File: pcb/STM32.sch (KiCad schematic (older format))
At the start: 32 parts, among them J1 Conn_02x07_Odd_Even, Q5 2SC3325-Y, X1 ABM8G

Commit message: Added all connections between STM and AQH3223. added pin header with GPIO from STM
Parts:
- added J3: Conn_02x11_Odd_Even, Connector_PinHeader_2.54mm:PinHeader_2x11_P2.54mm_Vertical, symbol Connector_Generic:Conn_02x11_Odd_Even
- J1: value Conn_02x07_Odd_Even -> Conn_02x04_Odd_Even; footprint Connector_PinSocket_2.54mm:PinSocket_2x07_P2.54mm_Horizontal -> Connector_PinSocket_2.54mm:PinSocket_2x04_P2.54mm_Horizontal; symbol Connector_Generic:Conn_02x07_Odd_Even -> Connector_Generic:Conn_02x04_Odd_Even
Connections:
- net +3V3: now also J3.1 (Pin_1)
- net +5V: now also J3.2 (Pin_2)
- net GND: now also J1.7 (Pin_7), J1.8 (Pin_8), J3.20 (Pin_20), J3.21 (Pin_21), J3.22 (Pin_22); no longer J1.13 (Pin_13), J1.14 (Pin_14)
- net LED: now also UST1.7 (PC13); no longer UST1.48 (PB11/I2C2_SDA/USART3_TX/TIM2_CH4)
- net PA10: now also J3.17 (Pin_17); no longer J1.10 (Pin_10)
- net PA11: now also J3.18 (Pin_18); no longer J1.11 (Pin_11)
- net PA12: now also J3.19 (Pin_19); no longer J1.12 (Pin_12)
- net PA8: now also J3.15 (Pin_15); no longer J1.8 (Pin_8)
- net PA9: now also J3.16 (Pin_16); no longer J1.9 (Pin_9)
- net PC9: now also J3.14 (Pin_14); no longer J1.7 (Pin_7)
- net P_EV7: now reaches UST1.38 (PE7)
- net PD8: now reaches UST1.55 (PD8/USART3_TX)
- net PD8: now also J3.3 (Pin_3)
- net PD9: now reaches UST1.56 (PD9/USART3_RX)
- net PD9: now also J3.4 (Pin_4)
- net PD10: now reaches UST1.57 (PD10/USART3_CK)
- net PD10: now also J3.5 (Pin_5)
- net PD11: now reaches UST1.58 (PD11/USART3_CTS)
- net PD11: now also J3.6 (Pin_6)
- net PD12: now reaches UST1.59 (PD12/TIM4_CH1/USART3_RTS)
- net PD12: now also J3.7 (Pin_7)
- net PD13: now reaches UST1.60 (PD13/TIM4_CH2)
- net PD13: now also J3.8 (Pin_8)
- net PD14: now reaches UST1.61 (PD14/TIM4_CH3)
- net PD14: now also J3.9 (Pin_9)
- net PD15: now reaches UST1.62 (PD15/TIM4_CH4)
- net PD15: now also J3.10 (Pin_10)
- net PC6: now reaches UST1.63 (PC6/TIM8_CH1/SDIO_D6/USART6_TX//TIM3_CH1)
- net PC6: now also J3.11 (Pin_11)
- net PC7: now reaches UST1.64 (PC7/TIM8_CH2/SDIO_D7/USART6_RX/TIM3_CH2)
- net PC7: now also J3.12 (Pin_12)
- net PC8: now reaches UST1.65 (PC8/TIM8_CH3/SDIO_D0/TIM3_CH3/USART6_CK)
- net PC8: now also J3.13 (Pin_13)
- net PE0 renamed P_EV15
- net PE1 renamed P_EV14
- net PE2 renamed P_EV13
- net PE3 renamed P_EV12
- net PE4 renamed P_EV11
- net PE5 renamed P_EV10
- net PE6 renamed P_EV9
- net PE7 renamed P_EV8
- new net P_EV16: UST1.48 (PB11/I2C2_SDA/USART3_TX/TIM2_CH4)
- no-connect marks 30 -> 17
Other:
- moved on the sheet: FB1, R46, R47, R48, R49

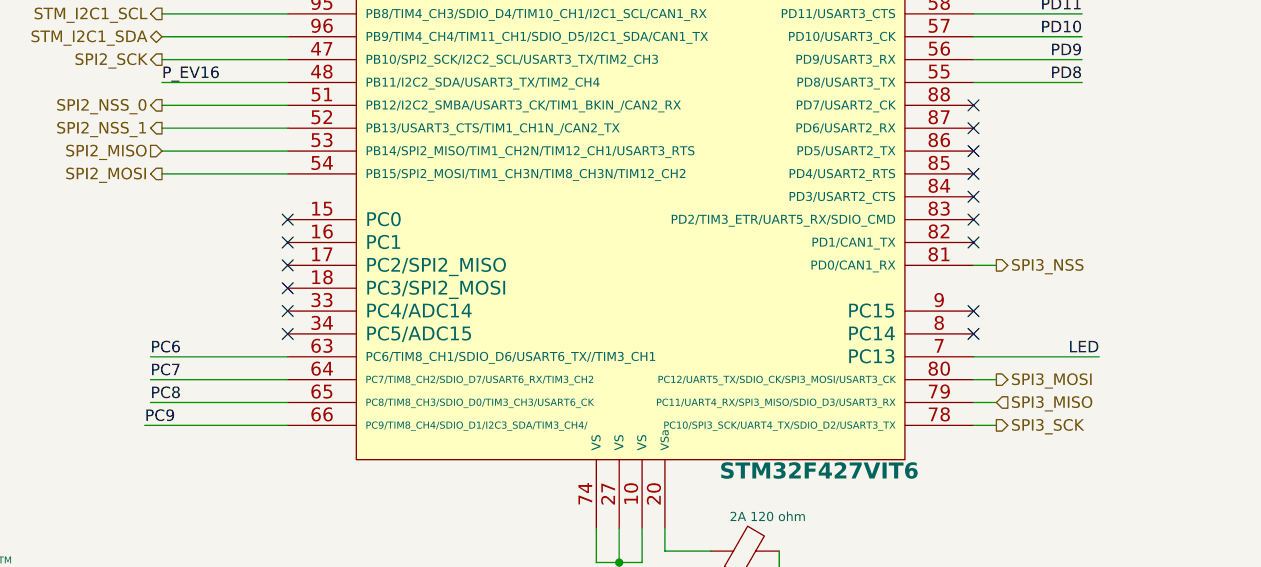
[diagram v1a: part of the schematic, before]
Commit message: Added 3d shape for connector clik-mate Added connection between STM and connector clik-mate on schema and PCB P3 is a connector that allows put a panic button for do a reset in the IC powerstep01
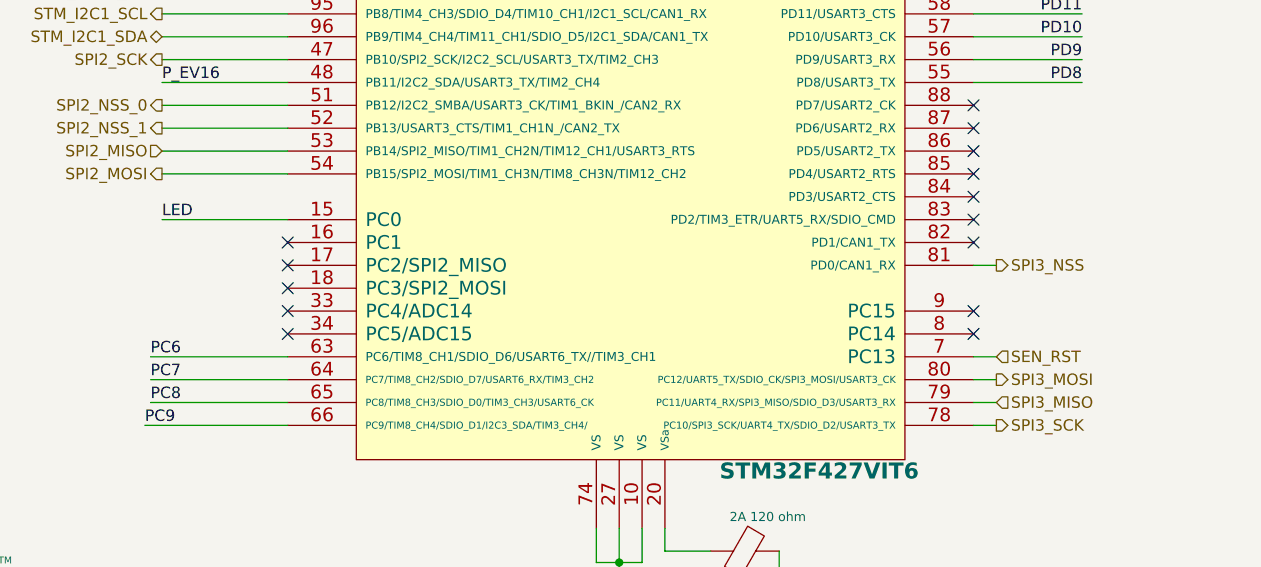
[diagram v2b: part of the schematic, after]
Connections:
- net LED: now also UST1.15 (PC0); no longer UST1.7 (PC13)
- new net SEN_RST: UST1.7 (PC13)
- no-connect marks 17 -> 16
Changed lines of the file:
@@
 NoConn ~ 5600 5600
 NoConn ~ 5600 5700
-NoConn ~ 2600 5200
 NoConn ~ 2600 5300
 NoConn ~ 2600 5400
@@
 $EndComp
 Wire Wire Line
-	5600 5800 6150 5800
-Text Label 6150 5800 2    50   ~ 0
+	2600 5200 2050 5200
+Text Label 2050 5200 0    50   ~ 0
 LED
 Entry Wire Line
@@
 	10325 3850 10325 3950
 Connection ~ 10325 3950
+Text HLabel 5700 5800 2    50   Input ~ 0
+SEN_RST
+Wire Wire Line
+	5700 5800 5600 5800
 Wire Bus Line
 	1800 6950 1800 7200

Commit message: Added components dikey part numbers in modified sheets
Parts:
- C29, C30, C38, CS1, CS2, CS3, CST1: DigiKey (none) -> 1276-1442-1-ND
- C39, CST2: DigiKey (none) -> 1276-1010-1-ND
- C40: DigiKey (none) -> 1276-1044-1-ND
- CST3, CST4: DigiKey (none) -> 1276-1469-1-ND
- CXST1, CXST2: DigiKey (none) -> 1276-1116-1-ND
- FB1, LST1, LST2: DigiKey (none) -> 445-2982-1-ND
- R25: DigiKey (none) -> P1.0KJCT-ND
- R46, R47, R48, R49: DigiKey (none) -> P100LCT-ND
- R54: DigiKey (none) -> P180JCT-ND
- RST1, RST2: DigiKey (none) -> 311-10KJRCT-ND
- X1: DigiKey (none) -> 535-14512-1-ND
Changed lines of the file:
@@
 F 2 "Capacitor_SMD:C_0402_1005Metric" H 1750 9050 60  0001 C CNN
 F 3 "" H 1750 9050 60  0001 C CNN
+F 4 "1276-1442-1-ND" H 1750 9050 50  0001 C CNN "DigiKey"
 	1    1750 9050
 	1    0    0    -1
@@
 F 2 "Capacitor_SMD:C_1206_3216Metric" H 3150 9050 60  0001 C CNN
 F 3 "" H 3150 9050 60  0001 C CNN
+F 4 "1276-1044-1-ND" H 3150 9050 50  0001 C CNN "DigiKey"
 	1    3150 9050
 	1    0    0    -1
@@
 F 2 "Capacitor_SMD:C_0603_1608Metric" H 2800 9050 60  0001 C CNN
 F 3 "" H 2800 9050 60  0001 C CNN
+F 4 "1276-1010-1-ND" H 2800 9050 50  0001 C CNN "DigiKey"
 	1    2800 9050
 	1    0    0    -1
@@
 F 2 "Capacitor_SMD:C_0402_1005Metric" H 2450 9050 60  0001 C CNN
 F 3 "" H 2450 9050 60  0001 C CNN
+F 4 "1276-1442-1-ND" H 2450 9050 50  0001 C CNN "DigiKey"
 	1    2450 9050
 	1    0    0    -1
@@
 F 2 "Capacitor_SMD:C_0402_1005Metric" H 2100 9050 60  0001 C CNN
 F 3 "" H 2100 9050 60  0001 C CNN
+F 4 "1276-1442-1-ND" H 2100 9050 50  0001 C CNN "DigiKey"
 	1    2100 9050
 	1    0    0    -1
@@
 F 2 "Capacitor_SMD:C_0402_1005Metric" H 1100 9050 60  0001 C CNN
 F 3 "" H 1100 9050 60  0001 C CNN
+F 4 "1276-1442-1-ND" H 1100 9050 50  0001 C CNN "DigiKey"
 	1    1100 9050
 	1    0    0    -1
@@
 F 2 "Capacitor_SMD:C_0402_1005Metric" H 1450 9050 60  0001 C CNN
 F 3 "" H 1450 9050 60  0001 C CNN
+F 4 "1276-1442-1-ND" H 1450 9050 50  0001 C CNN "DigiKey"
 	1    1450 9050
 	1    0    0    -1
@@
 F 2 "Capacitor_SMD:C_0402_1005Metric" H 7100 1950 60  0001 C CNN
 F 3 "" H 7100 1950 60  0001 C CNN
+F 4 "1276-1116-1-ND" H 7100 1950 50  0001 C CNN "DigiKey"
 	1    7100 1950
 	0    -1   -1   0
@@
 F 2 "Capacitor_SMD:C_0402_1005Metric" H 7100 1350 60  0001 C CNN
 F 3 "" H 7100 1350 60  0001 C CNN
+F 4 "1276-1116-1-ND" H 7100 1350 50  0001 C CNN "DigiKey"
 	1    7100 1350
 	0    -1   -1   0
@@
 F 2 "Resistor_SMD:R_0603_1608Metric" H 1050 850 60  0001 C CNN
 F 3 "" H 1050 850 60  0001 C CNN
+F 4 "445-2982-1-ND" V 1050 850 50  0001 C CNN "DigiKey"
 	1    1050 850
 	0    -1   -1   0
@@
 F 2 "Capacitor_SMD:C_0402_1005Metric" H 1350 950 60  0001 C CNN
 F 3 "" H 1350 950 60  0001 C CNN
+F 4 "1276-1442-1-ND" H 1350 950 50  0001 C CNN "DigiKey"
 	1    1350 950
 	1    0    0    -1
@@
 F 2 "Capacitor_SMD:C_0402_1005Metric" H 1750 950 60  0001 C CNN
 F 3 "" H 1750 950 60  0001 C CNN
+F 4 "1276-1010-1-ND" H 1750 950 50  0001 C CNN "DigiKey"
 	1    1750 950
 	1    0    0    -1
@@
 F 2 "Capacitor_SMD:C_0402_1005Metric" H 6200 1100 60  0001 C CNN
 F 3 "" H 6200 1100 60  0001 C CNN
+F 4 "1276-1469-1-ND" H 6200 1100 50  0001 C CNN "DigiKey"
 	1    6200 1100
 	1    0    0    -1
@@
 F 2 "Resistor_SMD:R_0402_1005Metric" H 1300 7450 60  0001 C CNN
 F 3 "" H 1300 7450 60  0001 C CNN
+F 4 "311-10KJRCT-ND" V 1300 7450 50  0001 C CNN "DigiKey"
 	1    1300 7450
 	-1   0    0    1
@@
 F 2 "Resistor_SMD:R_0402_1005Metric" H 1300 7050 60  0001 C CNN
 F 3 "" H 1300 7050 60  0001 C CNN
+F 4 "311-10KJRCT-ND" V 1300 7050 50  0001 C CNN "DigiKey"
 	1    1300 7050
 	-1   0    0    -1
@@
 F 2 "Capacitor_SMD:C_0402_1005Metric" H 6000 1100 60  0001 C CNN
 F 3 "" H 6000 1100 60  0001 C CNN
+F 4 "1276-1469-1-ND" H 6000 1100 50  0001 C CNN "DigiKey"
 	1    6000 1100
 	1    0    0    -1
@@
 F 2 "Capacitor_SMD:C_0402_1005Metric" H 3500 9050 60  0001 C CNN
 F 3 "" H 3500 9050 60  0001 C CNN
+F 4 "1276-1442-1-ND" H 3500 9050 50  0001 C CNN "DigiKey"
 	1    3500 9050
 	1    0    0    -1
@@
 F 2 "Resistor_SMD:R_0603_1608Metric" V 10405 2075 50  0001 C CNN
 F 3 "~" H 10475 2075 50  0001 C CNN
+F 4 "445-2982-1-ND" V 10475 2075 50  0001 C CNN "DigiKey"
 	1    10475 2075
 	0    1    1    0
@@
 F 2 "Resistor_SMD:R_0603_1608Metric" H 4600 6650 60  0001 C CNN
 F 3 "" H 4600 6650 60  0001 C CNN
+F 4 "445-2982-1-ND" V 4600 6650 50  0001 C CNN "DigiKey"
 	1    4600 6650
 	0    -1   -1   0
@@
 F 2 "SMD:ABM8G" H 6750 1650 50  0001 C CNN
 F 3 "" H 6750 1650 50  0001 C CNN
+F 4 "535-14512-1-ND" V 6750 1650 50  0001 C CNN "DigiKey"
 	1    6750 1650
 	0    -1   -1   0
@@
 F 2 "Resistor_SMD:R_0402_1005Metric" V 9430 4750 50  0001 C CNN
 F 3 "~" H 9500 4750 50  0001 C CNN
+F 4 "P100LCT-ND" V 9500 4750 50  0001 C CNN "DigiKey"
 	1    9500 4750
 	0    1    1    0
@@
 F 2 "Resistor_SMD:R_0402_1005Metric" V 9430 4650 50  0001 C CNN
 F 3 "~" H 9500 4650 50  0001 C CNN
+F 4 "P100LCT-ND" V 9500 4650 50  0001 C CNN "DigiKey"
 	1    9500 4650
 	0    1    1    0
@@
 F 2 "Resistor_SMD:R_0402_1005Metric" V 10580 4750 50  0001 C CNN
 F 3 "~" H 10650 4750 50  0001 C CNN
+F 4 "P100LCT-ND" V 10650 4750 50  0001 C CNN "DigiKey"
 	1    10650 4750
 	0    1    1    0
@@
 F 2 "Resistor_SMD:R_0402_1005Metric" V 10580 4650 50  0001 C CNN
 F 3 "~" H 10650 4650 50  0001 C CNN
+F 4 "P100LCT-ND" V 10650 4650 50  0001 C CNN "DigiKey"
 	1    10650 4650
 	0    1    1    0
@@
 F 2 "Resistor_SMD:R_0402_1005Metric" V 9055 6475 50  0001 C CNN
 F 3 "~" H 9125 6475 50  0001 C CNN
+F 4 "P180JCT-ND" V 9125 6475 50  0001 C CNN "DigiKey"
 	1    9125 6475
 	0    1    1    0
@@
 F 2 "Resistor_SMD:R_0402_1005Metric" V 10630 5725 50  0001 C CNN
 F 3 "~" H 10700 5725 50  0001 C CNN
-F 4 "" V 10700 5725 50  0001 C CNN "DigiKey"
+F 4 "P1.0KJCT-ND" V 10700 5725 50  0001 C CNN "DigiKey"
 	1    10700 5725
 	0    1    1    0
@@
 F 2 "Connector_PinHeader_2.54mm:PinHeader_2x11_P2.54mm_Vertical" H 10025 3450 50  0001 C CNN
 F 3 "~" H 10025 3450 50  0001 C CNN
+F 4 "" H 10025 3450 50  0001 C CNN "DigiKey"
 	1    10025 3450
 	1    0    0    -1

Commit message: Added digiKey part number for some components
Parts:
- J3: DigiKey (none) -> S2012EC-40-ND
- RST1, RST2: DigiKey 311-10KJRCT-ND -> P10KJDKR-ND
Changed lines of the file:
@@
 F 2 "Resistor_SMD:R_0402_1005Metric" H 1300 7450 60  0001 C CNN
 F 3 "" H 1300 7450 60  0001 C CNN
-F 4 "311-10KJRCT-ND" V 1300 7450 50  0001 C CNN "DigiKey"
+F 4 "P10KJDKR-ND" V 1300 7450 50  0001 C CNN "DigiKey"
 	1    1300 7450
 	-1   0    0    1
@@
 F 2 "Resistor_SMD:R_0402_1005Metric" H 1300 7050 60  0001 C CNN
 F 3 "" H 1300 7050 60  0001 C CNN
-F 4 "311-10KJRCT-ND" V 1300 7050 50  0001 C CNN "DigiKey"
+F 4 "P10KJDKR-ND" V 1300 7050 50  0001 C CNN "DigiKey"
 	1    1300 7050
 	-1   0    0    -1
@@
 F 2 "Connector_PinHeader_2.54mm:PinHeader_2x11_P2.54mm_Vertical" H 10025 3450 50  0001 C CNN
 F 3 "~" H 10025 3450 50  0001 C CNN
-F 4 "" H 10025 3450 50  0001 C CNN "DigiKey"
+F 4 "S2012EC-40-ND" H 10025 3450 50  0001 C CNN "DigiKey"
 	1    10025 3450
 	1    0    0    -1

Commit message: Added all references on silkscreen added BOM for sensor modules
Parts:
- J1: DigiKey (none) -> 609-6367-ND‎
- LS1: DigiKey (none) -> 102-2196-1-ND; Field4 None -> (none); Field5 CUI -> (none); Field6 None -> (none); Field7 Unavailable -> (none)
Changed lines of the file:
@@
 F 2 "Connector_PinSocket_2.54mm:PinSocket_2x04_P2.54mm_Horizontal" H 10025 4650 50  0001 C CNN
 F 3 "~" H 10025 4650 50  0001 C CNN
+F 4 "609-6367-ND‎" H 10025 4650 50  0001 C CNN "DigiKey"
 	1    10025 4650
 	1    0    0    -1
@@
 F 2 "SMD:CUI_CSS-95B30-SMT" H 9525 5900 50  0001 L BNN
 F 3 "CSS-95B30-SMT" H 9525 5900 50  0001 L BNN
-F 4 "None" H 9525 5900 50  0001 L BNN "Field4"
-F 5 "CUI" H 9525 5900 50  0001 L BNN "Field5"
-F 6 "None" H 9525 5900 50  0001 L BNN "Field6"
-F 7 "Unavailable" H 9525 5900 50  0001 L BNN "Field7"
-F 8 "10 mm, 5 V, 92 dB, Surface Mount _SMT_, Magnetic Audio Transducer Buzzer" H 9525 5900 50  0001 L BNN "Field8"
+F 4 "102-2196-1-ND" H 9525 5900 50  0001 C CNN "DigiKey"
+F 5 "10 mm, 5 V, 92 dB, Surface Mount _SMT_, Magnetic Audio Transducer Buzzer" H 9525 5900 50  0001 L BNN "Field8"
 	1    9525 5900
 	1    0    0    -1
